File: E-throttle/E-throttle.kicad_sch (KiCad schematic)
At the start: 43 parts, among them IC1 BTS441TG, J1 PROG, J2 JTAG, J3 Conn_01x11, J4 Conn_01x11, J5 776087-1, J6 Conn_01x15, J7 Conn_01x15, Q1 NMOS, SW1 SW_Push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

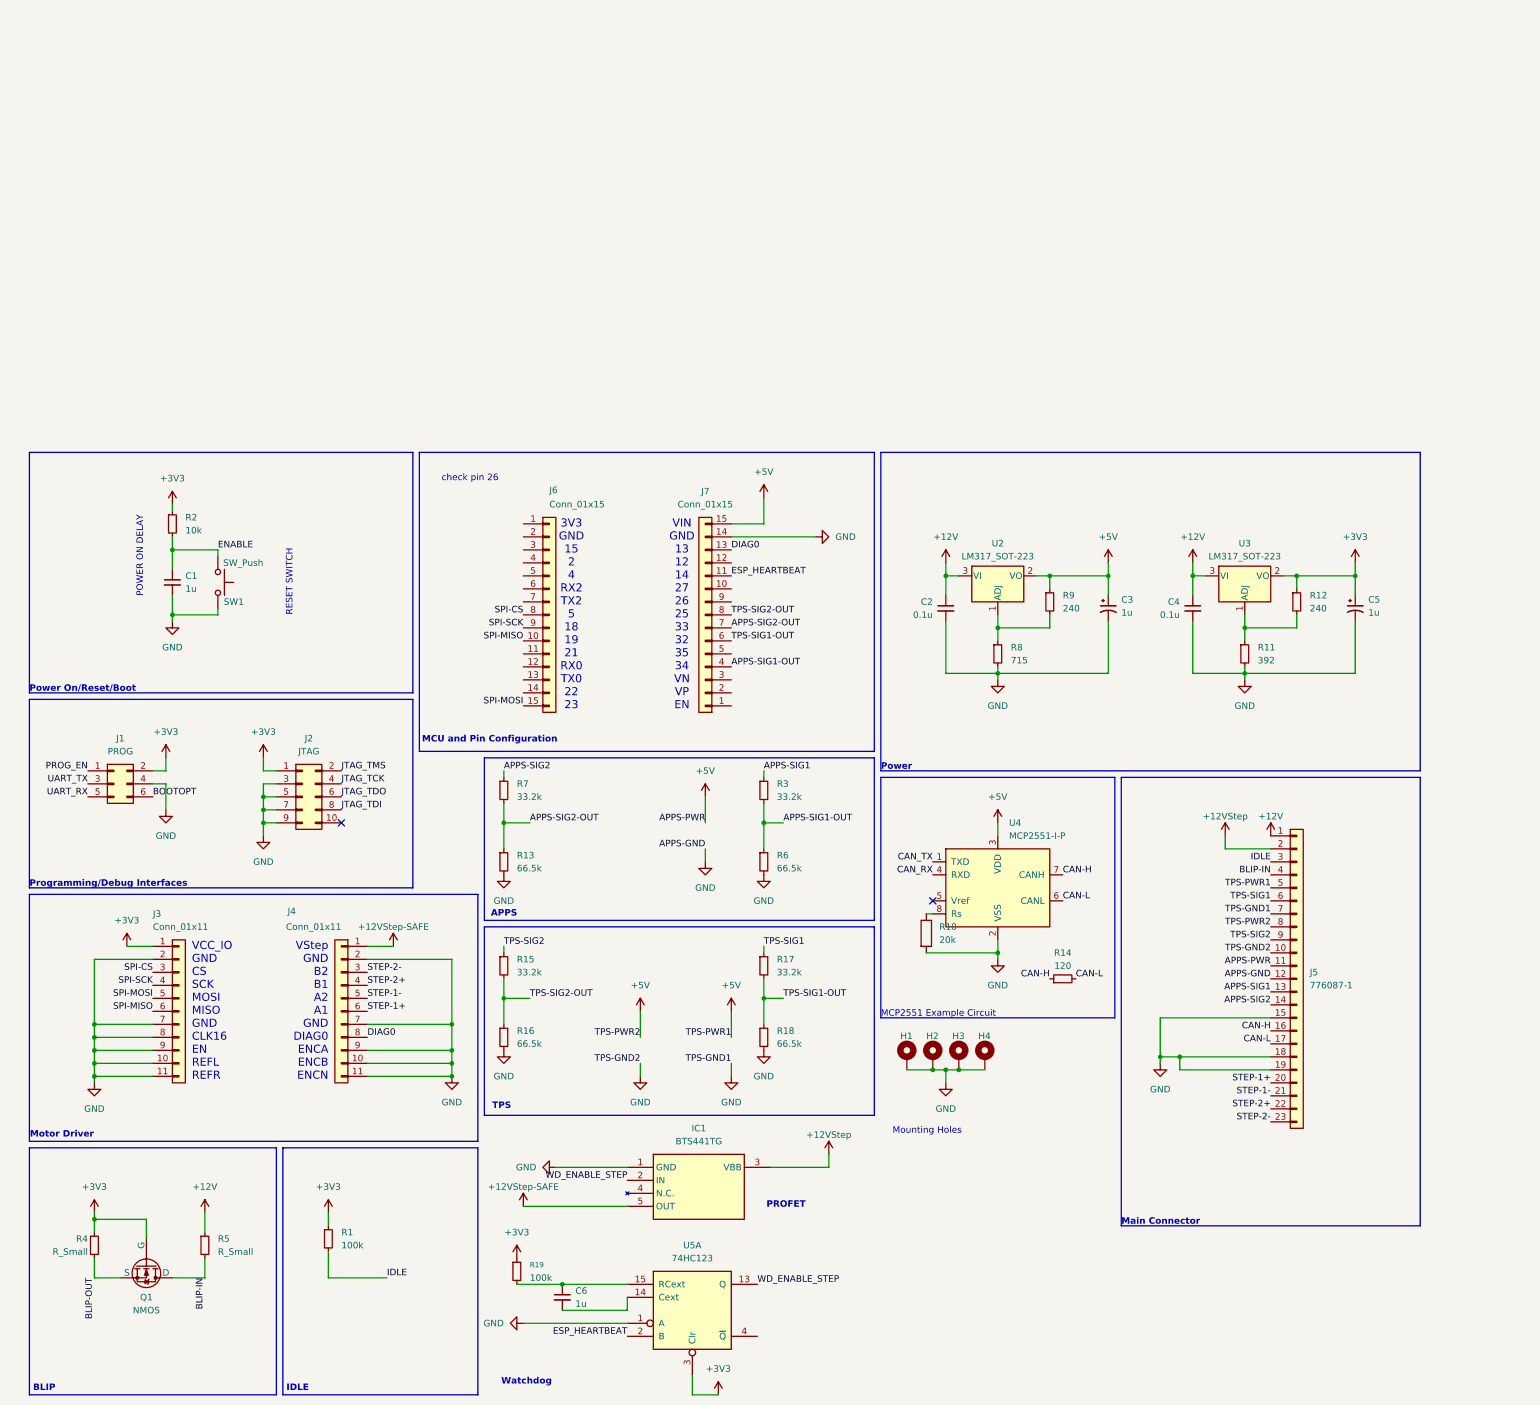
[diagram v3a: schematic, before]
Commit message: Updated schematic based on today's discussions
Updated:
- Second Watchdog with independent ESP heartbeat
- Relay pins (21 and 22) from connector
- BLIP and IDLE connected to ESP GPIO pins

Not Added Yet:
- Relay
- Status LEDs
- SD Card
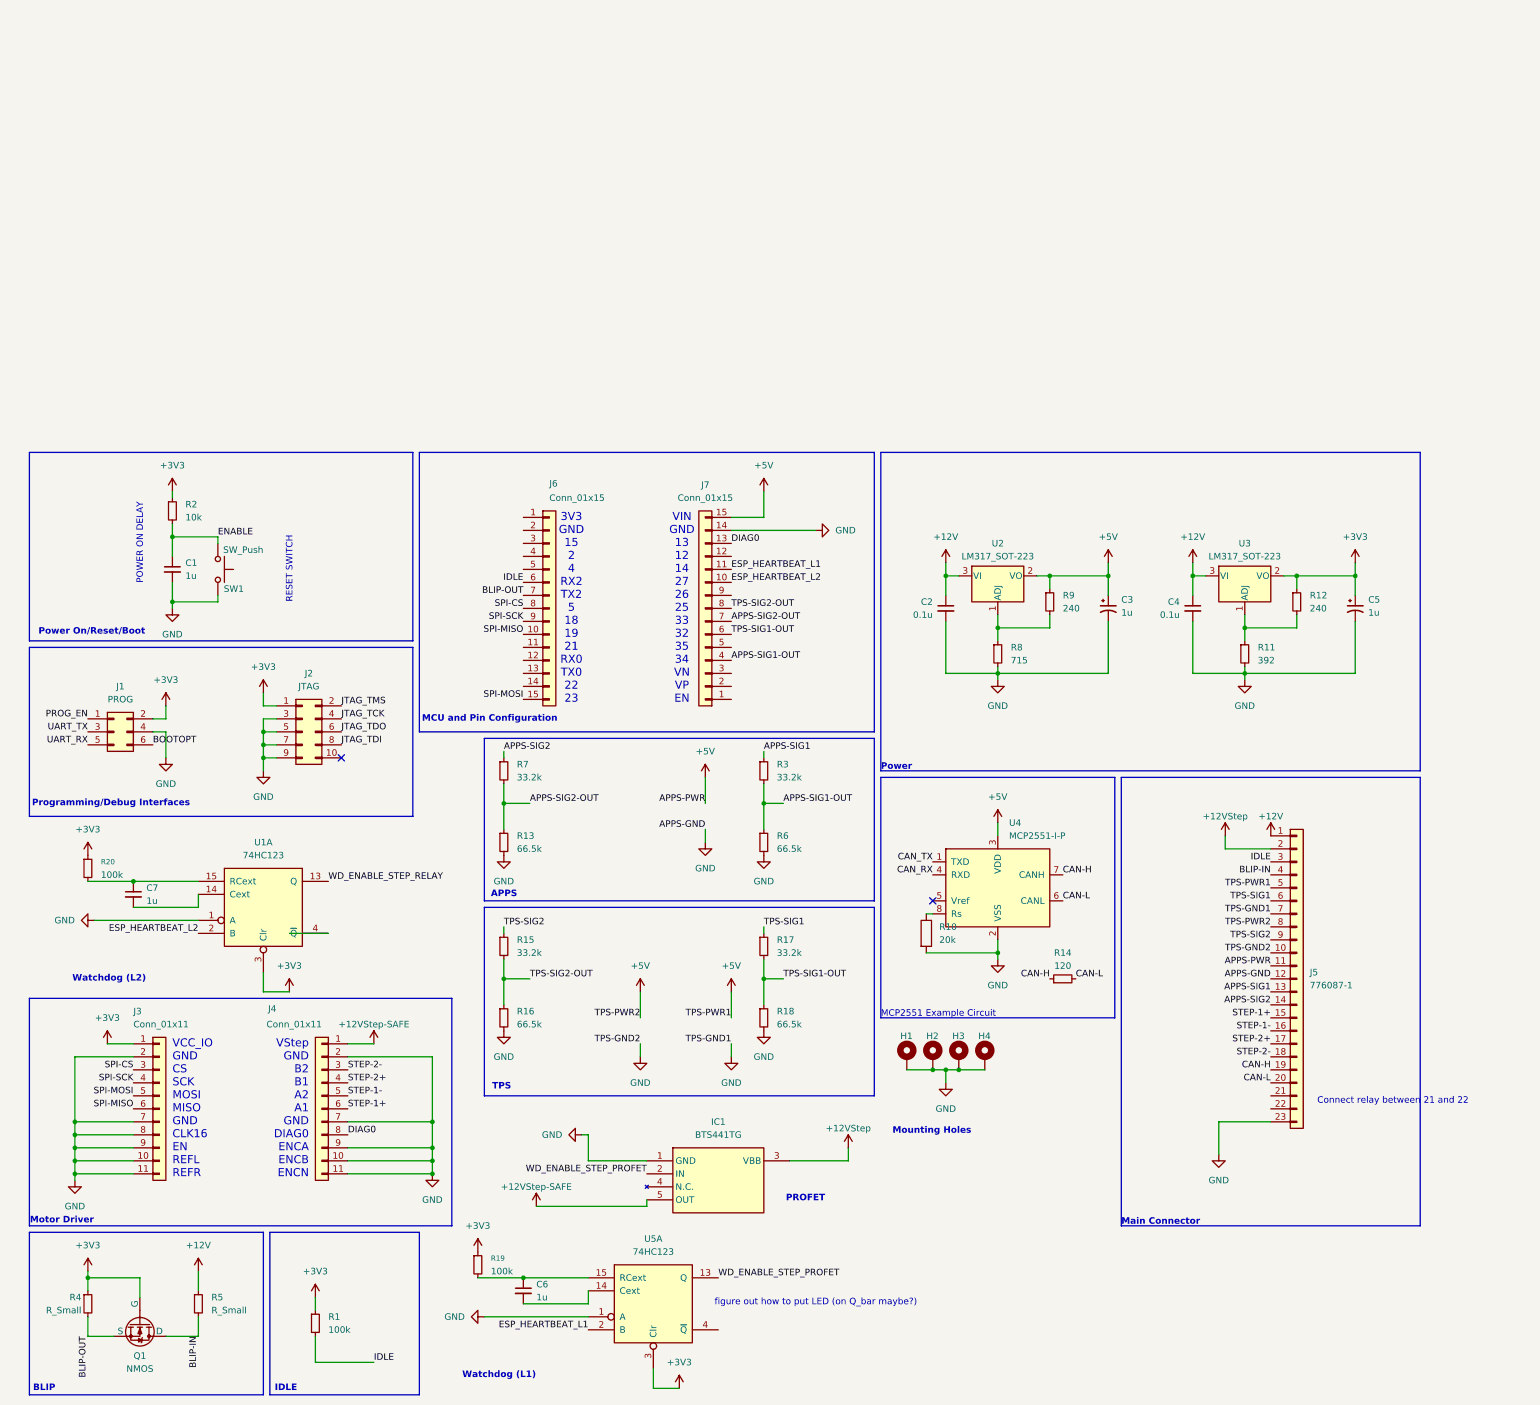
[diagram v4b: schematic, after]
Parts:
- added C7: 1u, Capacitor_THT:C_Disc_D5.0mm_W2.5mm_P2.50mm, symbol Device:C_Small
- added R20: 100k, Resistor_THT:R_Axial_DIN0207_L6.3mm_D2.5mm_P10.16mm_Horizontal, symbol Device:R_Small
- added U1: 74HC123, symbol 74xx:74HC123
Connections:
- net +3V3: now also R20.1, U1.3 (Clr)
- net BLIP-OUT: now also J6.7 (Pin_7)
- net CAN-H: now also J5.19 (Pin_19); no longer J5.16 (Pin_16)
- net CAN-L: now also J5.20 (Pin_20); no longer J5.17 (Pin_17)
- net GND: now also J5.23 (Pin_23), U1.1 (A); no longer J5.15 (Pin_15), J5.18 (Pin_18), J5.19 (Pin_19)
- net IDLE: now also J6.6 (Pin_6)
- net STEP-1+: now also J5.15 (Pin_15); no longer J5.20 (Pin_20)
- net STEP-1-: now also J5.16 (Pin_16); no longer J5.21 (Pin_21)
- net STEP-2+: now also J5.17 (Pin_17); no longer J5.22 (Pin_22)
- net STEP-2-: now also J5.18 (Pin_18); no longer J5.23 (Pin_23)
- net ESP_HEARTBEAT_L2: now reaches J7.10 (Pin_10)
- net ESP_HEARTBEAT_L2: now also U1.2 (B)
- net ESP_HEARTBEAT renamed ESP_HEARTBEAT_L1
- net WD_ENABLE_STEP renamed WD_ENABLE_STEP_PROFET
- new net: C7.1, R20.2, U1.15 (RCext)
- new net: C7.2, U1.14 (Cext)
- new net WD_ENABLE_STEP_RELAY: U1.13 (Q)
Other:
- note added: "Connect relay between 21 and 22"
- note added: "Watchdog (L1)"
- note added: "Watchdog (L2)"
- note added: "figure out how to put LED (on Q_bar maybe?)"
- note removed: "Watchdog"
- note removed: "check pin 26"
- moved on the sheet: C1, C6, IC1, J1, J2, J3, J4, J6, J7, Q1, R1, R13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

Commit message: Added MicroSD Card to schematic
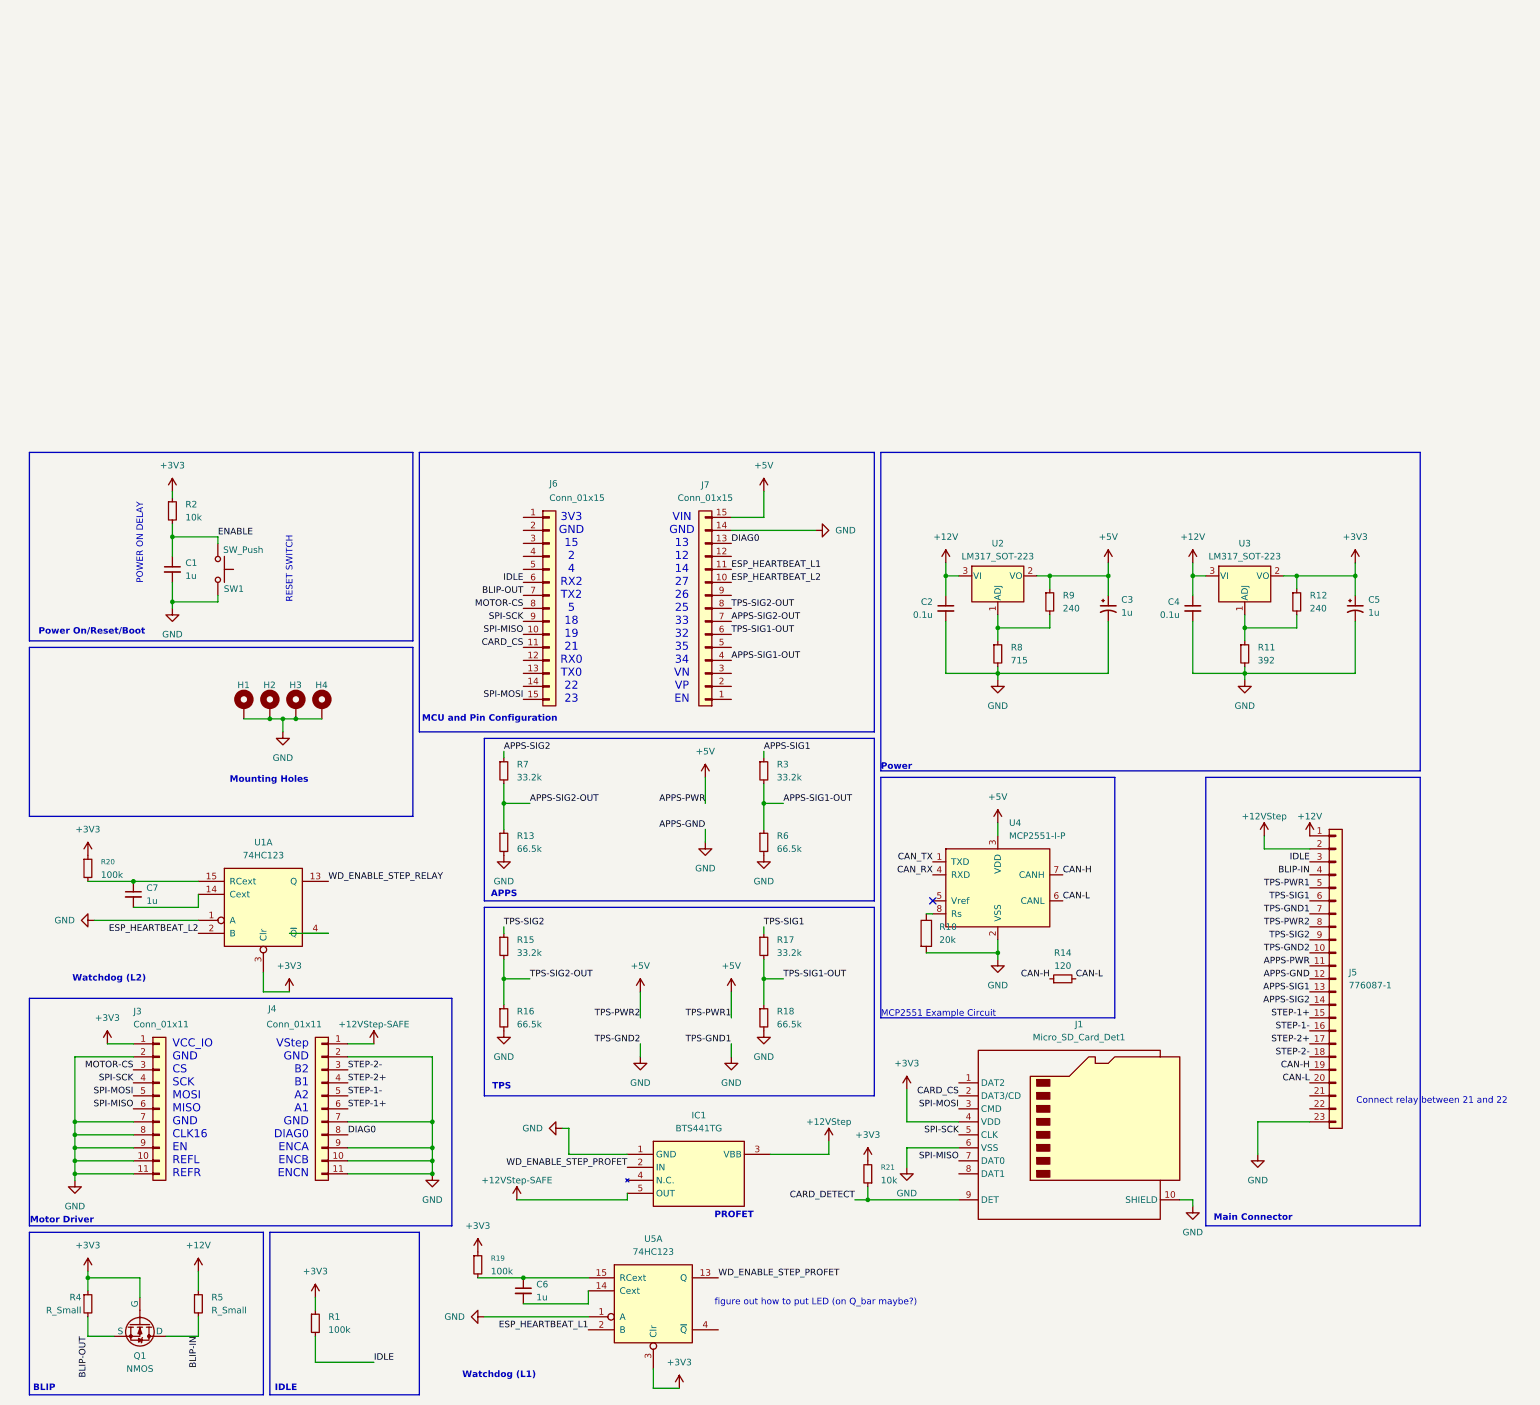
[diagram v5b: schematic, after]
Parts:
- removed J1: PROG, Connector_PinSocket_2.54mm:PinSocket_2x03_P2.54mm_Vertical, symbol Connector_Generic:Conn_02x03_Odd_Even
- removed J2: JTAG, Connector_PinSocket_2.54mm:PinSocket_2x05_P2.54mm_Vertical, symbol Connector_Generic:Conn_02x05_Odd_Even
- added J1: Micro_SD_Card_Det1, symbol Connector:Micro_SD_Card_Det1
- added R21: 10k, symbol Device:R_Small
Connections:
- net +3V3: now also J1.4 (VDD), R21.2
- net GND: now also J1.10 (SHIELD), J1.6 (VSS)
- net SPI-MISO: now also J1.7 (DAT0)
- net SPI-MOSI: now also J1.3 (CMD)
- net SPI-SCK: now also J1.5 (CLK)
- net CARD_CS: now reaches J6.11 (Pin_11)
- net CARD_CS: now also J1.2 (DAT3/CD)
- net SPI-CS renamed MOTOR-CS
- new net CARD_DETECT: J1.9 (DET), R21.1
- no-connect marks 2 -> 1
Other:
- note removed: "Programming/Debug Interfaces"
- moved on the sheet: H1, H2, H3, H4, IC1, J5

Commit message: Added status LEDs, reorganized schematic
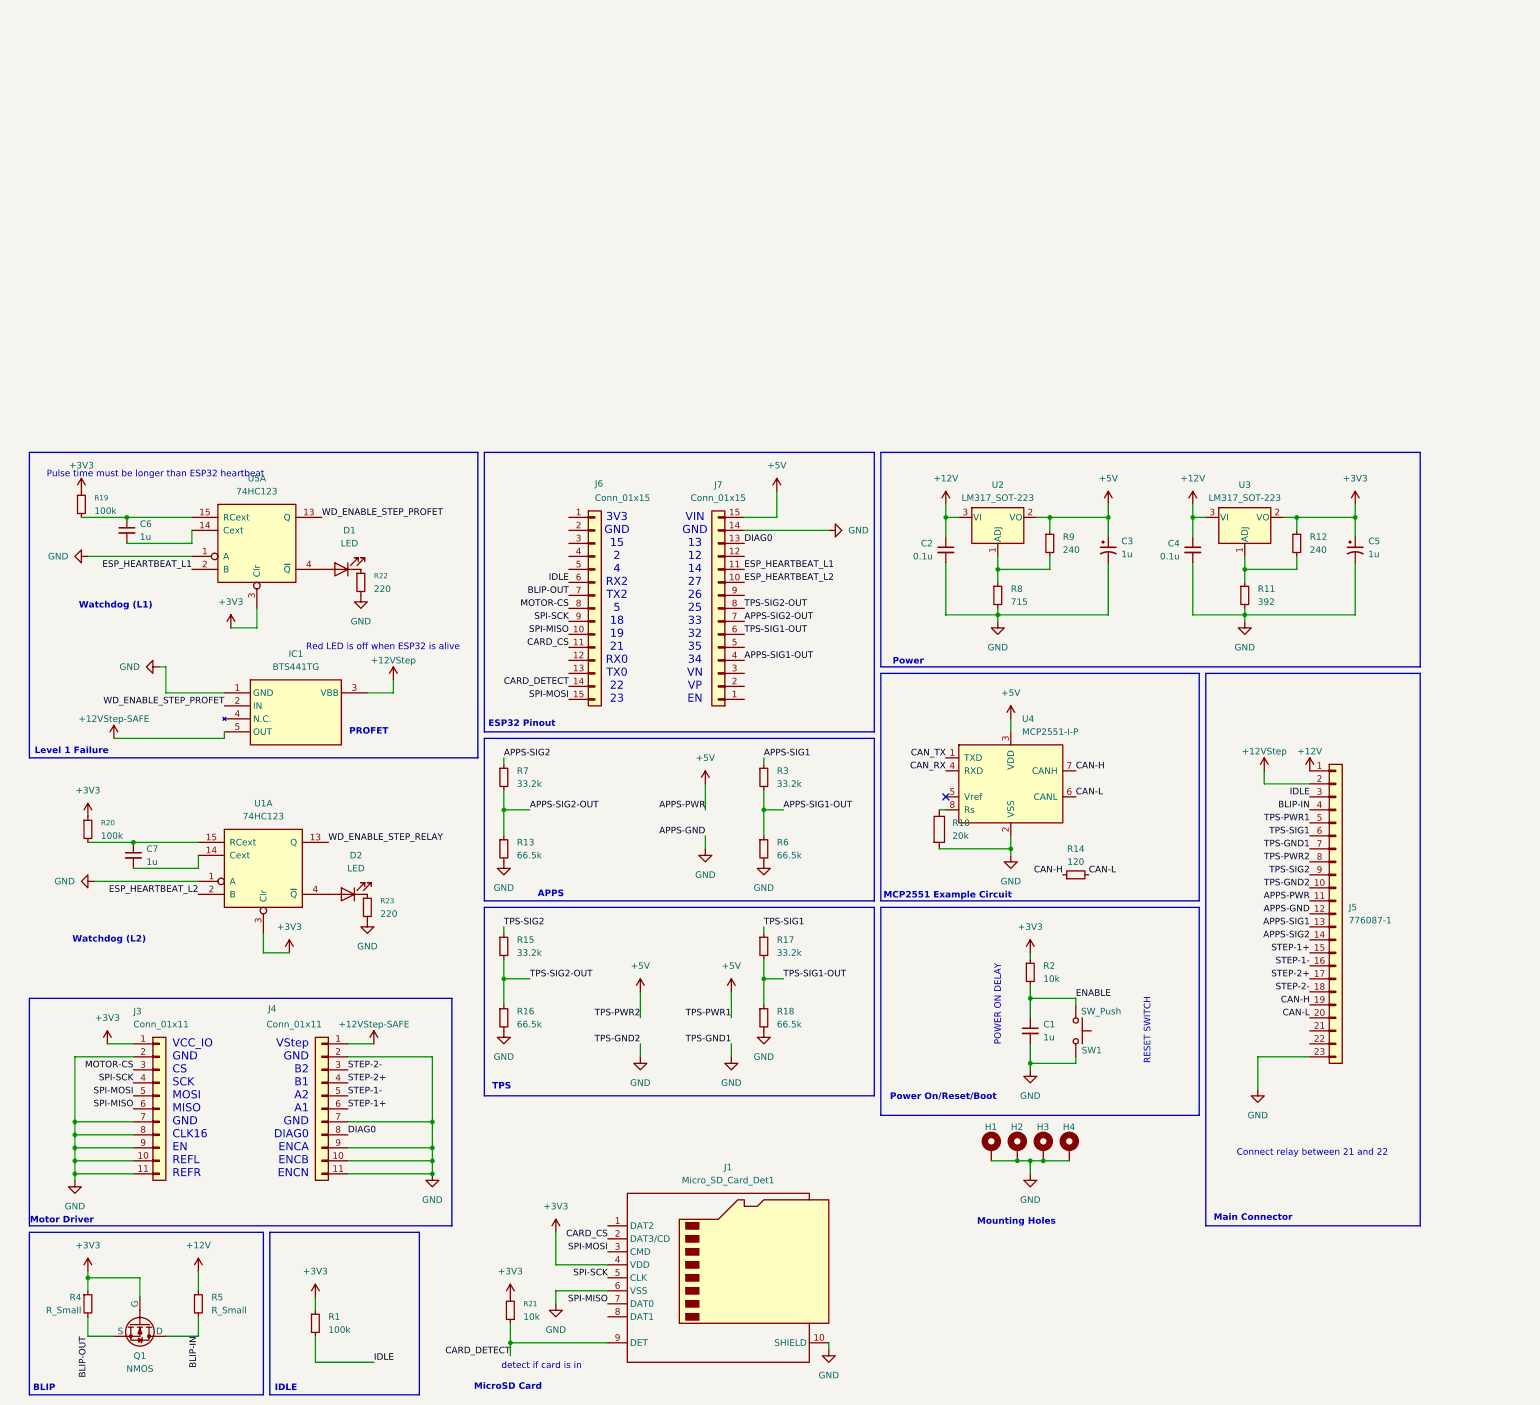
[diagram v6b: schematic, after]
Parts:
- added D1, D2: LED, symbol Device:LED
- added R22, R23: 220, symbol Device:R_Small
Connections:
- net CARD_DETECT: now also J6.14 (Pin_14)
- net GND: now also R22.2, R23.2
- net at U5.4 (~{Q}): now also D1.2 (A)
- net at U1.4 (~{Q}): now also D2.2 (A)
- new net: D2.1 (K), R23.1
- new net: D1.1 (K), R22.1
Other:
- note added: "ESP32 Pinout"
- note added: "Level 1 Failure"
- note added: "MicroSD Card"
- note added: "Pulse time must be longer than ESP32 heartbeat"
- note added: "Red LED is off when ESP32 is alive"
- note added: "detect if card is in"
- note removed: "MCU and Pin Configuration"
- note removed: "figure out how to put LED (on Q_bar maybe?)"
- moved on the sheet: C1, C2, C3, C4, C5, C6, C7, H1, H2, H3, H4, IC1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
